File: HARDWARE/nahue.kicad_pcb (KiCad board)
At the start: 2 copper layers, 42 parts, among them J1 Conn_01x15, J2 Screw_Terminal_01x03, J3 Screw_Terminal_01x03, J4 Screw_Terminal_01x03, J5 bateria, J6 Screw_Terminal_01x03, J7 Conn_01x15, K1 JQC-3FF-005-1Z, K2 JQC-3FF-005-1Z, K3 JQC-3FF-005-1Z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

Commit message: actualizacion de kicad
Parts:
- added U6: LM7805_TO220, Package_TO_SOT_THT:TO-220-3_Vertical, F.Cu at (98.7, 20.2)
- J2, J3, J4, J5, J6, K1, K2, K3, K4: moved to F.Cu
- U5: value KA78M05_TO252 -> ESP32-S2-WROVER; footprint Package_TO_SOT_SMD:TO-252-2 -> RF_Module:ESP32-S2-WROVER; moved to F.Cu
- moved U5 152.8 mm to (18.4, 29.9)
- moved J5 95.2 mm to (86.5, 25.2)
- moved K3 74.6 mm to (110.0, 109.0)
- moved J4 72.6 mm to (86.9, 108.0), turned to 90 degrees
- moved D1 67.2 mm to (127.8, 100.8), turned to 0 degrees
- moved D2 66.4 mm to (117.0, 103.2), turned to 90 degrees
- moved R3 65.8 mm to (122.4, 100.8)
- moved Q3 63.1 mm to (122.4, 105.5)
- moved R2 62.9 mm to (128.3, 104.6)
- moved U3 62.1 mm to (139.7, 102.0), turned to 180 degrees
- moved R10 57.4 mm to (148.4, 43.9), turned to 180 degrees
- moved R1 57.2 mm to (148.4, 100.8), turned to 180 degrees
- moved R11 53.8 mm to (127.9, 47.8)
- moved Q1 53.8 mm to (122.4, 48.7)
- moved U1 53.3 mm to (138.9, 45.2), turned to 180 degrees
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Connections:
- C1 pad 1: VIN -> Net-(J5-Pin_2)
- C1 pad 2: GND -> Net-(U6-VI)
- R10 pad 1: D21 -> D22
- R4 pad 2: D5 -> D19
- R7 pad 2: D19 -> D21
- U5 pad 1: Net-(J5-Pin_2) -> Net-(U5-GND-Pad1)
- U5 pad 2: GND -> unconnected-(U5-3V3-Pad2)
- U5 pad 3: VIN -> unconnected-(U5-IO00-Pad3)
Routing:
- net VIN: track 229.6 -> 445.2 mm
- net D18: track 0.00 -> 58.6 mm
- net Net-(J5-Pin_2): track 18.1 -> 68.9 mm
- net D19: track 0.00 -> 43.3 mm
- net Net-(U6-VI): track 0.00 -> 32.8 mm
- net D21: track 0.00 -> 32.2 mm
- net D22: track 0.00 -> 23.9 mm
- net Net-(D4-A): track 34.0 -> 18.9 mm
- net Net-(D6-A): track 34.0 -> 18.9 mm
- net Net-(D2-A): track 33.4 -> 19.4 mm
- net Net-(D8-A): track 32.9 -> 19.0 mm
- net GND: track 9.51 -> 18.7 mm
- net COM2: track 35.2 -> 30.1 mm
- net COM3: track 34.2 -> 30.1 mm
- net Net-(R8-Pad1): track 10.1 -> 6.39 mm
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
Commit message: modificacion del kicad
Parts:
- removed U5: ESP32-S2-WROVER, RF_Module:ESP32-S2-WROVER

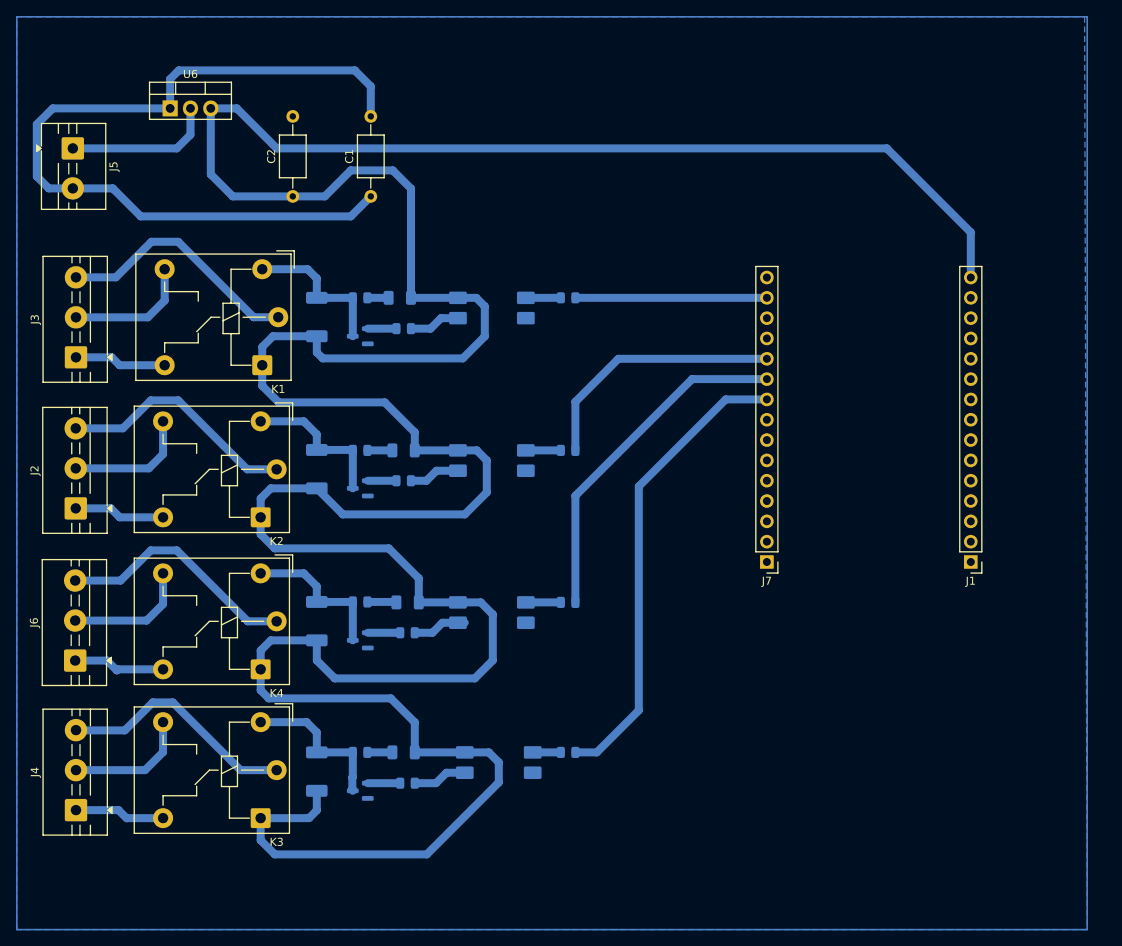
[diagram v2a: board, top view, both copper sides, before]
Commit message: se agrego huella del ESP32(falta terminar)
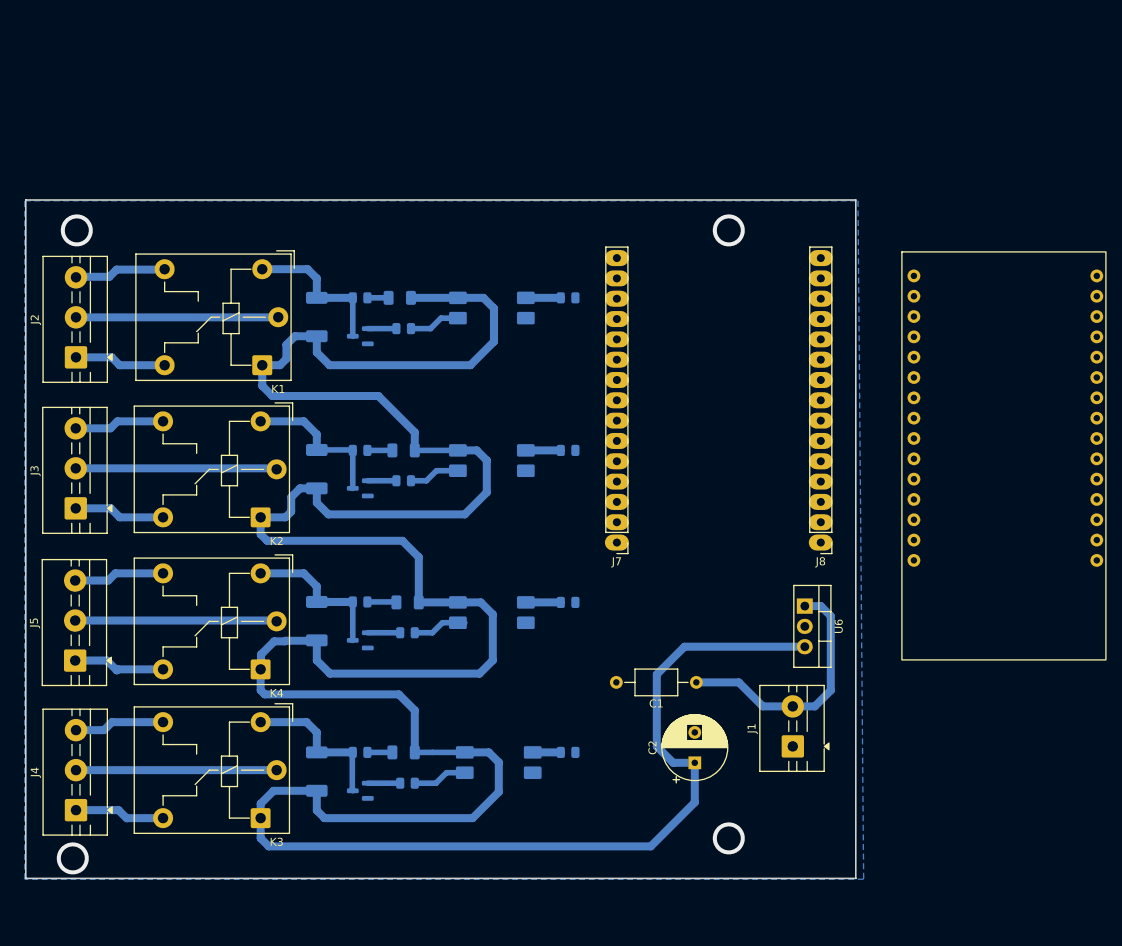
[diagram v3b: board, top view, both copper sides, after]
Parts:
- removed the J5 at (86.5, 25.2)
- added J1: ~, TerminalBlock:TerminalBlock_MaiXu_MX126-5.0-02P_1x02_P5.00mm, F.Cu at (176.5, 100.0)
- added U5: ~, esp32-30pines:esp32, F.Cu at (191.6, 41.2)
- C1: value C_Small -> ~
- C2: value C_Small -> ~; footprint Capacitor_THT:C_Axial_L5.1mm_D3.1mm_P10.00mm_Horizontal -> Capacitor_THT:CP_Radial_D8.0mm_P3.80mm
- J3: renamed from J2; value Screw_Terminal_01x03 -> ~
- moved U6 100.8 mm to (178.0, 82.5), turned to -90 degrees
- moved C2 86.8 mm to (164.2, 102.1)
- moved C1 73.1 mm to (164.4, 92.0), turned to 180 degrees
- moved J7 18.9 mm to (154.5, 74.5)
- moved J8 18.9 mm to (180.0, 74.5)
- renumbered J3 to J2, J6 to J5, J1 to J8
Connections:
- C1 pad 1: Net-(J5-Pin_2) -> Net-(J1-Pin_2)
- C1 pad 2: Net-(U6-VI) -> GND
- J2 pad 2: NC1 -> COM1
- J2 pad 3: COM1 -> NC1
- J3 pad 2: NC2 -> COM2
- J3 pad 3: COM2 -> NC2
- J4 pad 2: NC3 -> COM3
- J4 pad 3: COM3 -> NC3
- J5 pad 2: NC4 -> COM4
- J5 pad 3: COM4 -> NC4
- R10 pad 1: D22 -> TX0
- R7 pad 2: D21 -> RX0
- U6 pad 1: Net-(U6-VI) -> Net-(J1-Pin_2)
- U6 pad 3: Net-(U6-VO) -> VIN
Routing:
- net Net-(J5-Pin_2): track 68.9 -> 0.00 mm
- net VIN: track 445.2 -> 383.6 mm
- net D18: track 58.6 -> 0.00 mm
- net D19: track 43.3 -> 0.00 mm
- net Net-(U6-VI): track 32.8 -> 0.00 mm
- net D21: track 32.2 -> 0.00 mm
- net Net-(J1-Pin_2): track 0.00 -> 31.9 mm
- net D22: track 23.9 -> 0.00 mm
- net GND: track 18.7 -> 0.00 mm, vias 0 -> 4
- net COM1: track 31.0 -> 25.3 mm
- net COM4: track 30.4 -> 25.2 mm
- net COM3: track 30.1 -> 25.1 mm
- net COM2: track 30.1 -> 25.2 mm
- net NC1: track 15.9 -> 11.4 mm
- net NC2: track 15.8 -> 11.3 mm
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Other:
- board outline added: 103.8 x 84.8 mm

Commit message: últimos arreglos 1
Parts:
- removed J7, J8: Conn_01x15, Connector_PinHeader_2.54mm:PinHeader_1x15_P2.54mm_Vertical
- moved U5 37.6 mm to (174.4, 74.6), turned to 180 degrees
- moved C2 9.78 mm to (154.6, 103.8)
- moved J1 9.78 mm to (166.9, 101.8)
- moved U6 9.78 mm to (168.4, 84.2)
- moved R7 8.07 mm to (141.8, 58.5), turned to 90 degrees
- moved R4 6.97 mm to (143.1, 77.5), turned to 90 degrees
- moved R10 6.93 mm to (143.1, 39.4), turned to -90 degrees
- moved C1 6.92 mm to (157.8, 94.0), turned to 90 degrees
- moved R1 6.45 mm to (144.0, 96.1), turned to -90 degrees
- moved D6 3.82 mm to (118.1, 69.0)
- moved U2 1.38 mm to (137.5, 64.3)
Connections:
- R10 pad 1: TX0 -> RX2
- R7 pad 2: RX0 -> DX2
- U5 pad 1: unconnected-(U5-3V3-Pad1) -> EN
- U5 pad 10: unconnected-(U5-D19-Pad10) -> D27
- U5 pad 11: unconnected-(U5-D14-Pad11) -> D14
- U5 pad 12: unconnected-(U5-D12-Pad12) -> D12
- U5 pad 13: TX0 -> D13
- U5 pad 14: unconnected-(U5-D22-Pad14) -> GND
- U5 pad 15: unconnected-(U5-D23-Pad15) -> VIN
- U5 pad 2: unconnected-(U5-GND-Pad2) -> VP
- U5 pad 3: unconnected-(U5-D15-Pad3) -> VN
- U5 pad 4: unconnected-(U5-D2-Pad4) -> D34
- U5 pad 5: unconnected-(U5-D4-Pad5) -> D35
- U5 pad 6: unconnected-(U5-D32-Pad6) -> D32
- U5 pad 7: unconnected-(U5-D33-Pad7) -> D33
- U5 pad 8: unconnected-(U5-D5-Pad8) -> D25
- U5 pad 9: unconnected-(U5-D18-Pad9) -> D26
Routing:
- net D18: track 0.00 -> 45.0 mm
- net VIN: track 383.6 -> 414.1 mm
- net D19: track 0.00 -> 27.5 mm
- net RX2: track 0.00 -> 17.9 mm
- net DX2: track 0.00 -> 9.60 mm
- net Net-(D6-A): track 18.9 -> 24.8 mm
- net Net-(J1-Pin_2): track 31.9 -> 30.0 mm
- net Net-(R8-Pad1): track 6.39 -> 5.00 mm
- net Net-(R10-Pad2): track 4.37 -> 3.58 mm
- net Net-(R4-Pad1): track 4.37 -> 3.63 mm
- net Net-(R7-Pad1): track 4.37 -> 3.63 mm
- net GND: vias 4 -> 0
- net (no net): vias 0 -> 3
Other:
- board size 103.8 x 84.8 mm -> 97.2 x 84.8 mm

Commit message: retoques del kicad
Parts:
- moved D6 3.82 mm to (117.0, 65.3)
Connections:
- R10 pad 1: RX2 -> RX0
- R7 pad 2: DX2 -> TX0
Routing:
- net RX0: track 0.00 -> 32.4 mm
- net TX0: track 0.00 -> 23.9 mm
- net RX2: track 17.9 -> 0.00 mm
- net DX2: track 9.60 -> 0.00 mm
- net Net-(D6-A): track 24.8 -> 18.9 mm
- net VIN: track 414.1 -> 416.8 mm
- net D19: track 27.5 -> 26.3 mm
- net Net-(J1-Pin_2): track 30.0 -> 28.8 mm

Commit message: finalizando
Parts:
- added J6: Conn_01x08, Connector_PinSocket_2.54mm:PinSocket_1x08_P2.54mm_Vertical, F.Cu at (152.5, 81.8)
- K1, K2, K3, K4: value JQC-3FF-005-1Z -> RELAY
- moved U6 28.7 mm to (169.7, 112.8), turned to 180 degrees
- moved J1 17.3 mm to (153.7, 113.0), turned to 0 degrees
- moved C1 16.7 mm to (169.7, 105.8), turned to 180 degrees
- moved C2 11.8 mm to (147.0, 112.8), turned to 180 degrees
- moved R4 3.73 mm to (139.4, 77.5)
- moved R7 3.68 mm to (139.1, 55.9), turned to 0 degrees
- moved U2 3.01 mm to (134.8, 63.1), turned to -90 degrees
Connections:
- R1 pad 1: D18 -> D19
- R10 pad 1: RX0 -> RX2
- R4 pad 2: D19 -> D18
- R7 pad 2: TX0 -> DX2
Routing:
- net D2: track 0.00 -> 46.4 mm
- net D25: track 0.00 -> 32.4 mm
- net D32: track 0.00 -> 25.2 mm
- net D18: track 44.5 -> 24.0 mm
- net RX2: track 0.00 -> 17.7 mm
- net D22: track 0.00 -> 14.5 mm
- net VIN: track 416.8 -> 430.8 mm
- net VP: track 0.00 -> 13.1 mm
- net D19: track 26.3 -> 38.7 mm
- net DX2: track 0.00 -> 9.55 mm
- net RX0: track 32.4 -> 24.2 mm
- net Net-(J1-Pin_2): track 28.8 -> 22.5 mm
- net Net-(R8-Pad1): track 5.00 -> 11.1 mm
- net TX0: track 23.9 -> 19.6 mm
- net Net-(R7-Pad1): track 3.63 -> 7.46 mm
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- added copper zone on B.Cu, net (none)
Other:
- board size 97.2 x 84.8 mm -> 97.2 x 86.4 mm

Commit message: finalizado 2
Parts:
- added SW1: SW, Connector_PinHeader_2.54mm:PinHeader_1x02_P2.54mm_Vertical, F.Cu at (172.0, 97.8)
- moved J1 18.4 mm to (172.0, 110.8), turned to 90 degrees
- moved C2 9.82 mm to (152.6, 104.8)
- moved C1 8.10 mm to (162.8, 101.5), turned to 90 degrees
- moved U6 7.21 mm to (162.8, 110.8)
- moved R7 4.89 mm to (143.1, 58.7), turned to 90 degrees
- moved U2 4.31 mm to (138.9, 64.3), turned to 180 degrees
- moved R4 3.85 mm to (143.2, 77.7)
- moved R10 1.53 mm to (142.1, 40.6), turned to 0 degrees
- moved U4 0.12 mm to (139.0, 83.3)
- moved J5 0.10 mm to (86.9, 89.3)
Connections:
- C1 pad 1: Net-(J1-Pin_2) -> Net-(SW1A-B)
- R1 pad 1: D19 -> D23
- R4 pad 2: D18 -> D19
- U6 pad 1: Net-(J1-Pin_2) -> Net-(SW1A-B)
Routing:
- net D18: track 24.0 -> 0.00 mm
- net VIN: track 430.8 -> 407.2 mm
- net D23: track 0.00 -> 22.6 mm
- net D19: track 38.7 -> 18.2 mm
- net Net-(SW1A-B): track 0.00 -> 19.0 mm
- net Net-(J1-Pin_2): track 22.5 -> 8.01 mm
- net Net-(R8-Pad1): track 11.1 -> 6.37 mm
- net Net-(R7-Pad1): track 7.46 -> 3.42 mm
- net RX2: track 17.7 -> 21.1 mm
- net Net-(R4-Pad1): track 6.57 -> 3.42 mm
- net DX2: track 9.55 -> 8.30 mm
- net (no net): vias 2 -> 4

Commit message: duplicacion de placa
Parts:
- added C1: ~, Capacitor_THT:C_Axial_L5.1mm_D3.1mm_P10.00mm_Horizontal, F.Cu at (242.1, 130.2)
- added C2: ~, Capacitor_THT:CP_Radial_D8.0mm_P3.80mm, F.Cu at (231.9, 133.4)
- added D1: led smd 1206, LED_SMD:LED_1206_3216Metric, B.Cu at (207.2, 129.4)
- added D2: SM4007, Diode_SMD:D_MELF, B.Cu at (196.3, 131.8)
- added D3: led smd 1206, LED_SMD:LED_1206_3216Metric, B.Cu at (207.7, 110.7)
- added D4: SM4007, Diode_SMD:D_MELF, B.Cu at (196.3, 113.0)
- added D5: led smd 1206, LED_SMD:LED_1206_3216Metric, B.Cu at (207.2, 91.7)
- added D6: SM4007, Diode_SMD:D_MELF, B.Cu at (196.3, 94.0)
- added D7: led smd 1206, LED_SMD:LED_1206_3216Metric, B.Cu at (206.7, 72.6)
- added D8: SM4007, Diode_SMD:D_MELF, B.Cu at (196.3, 75.0)
- added J1: ~, TerminalBlock:TerminalBlock_MaiXu_MX126-5.0-02P_1x02_P5.00mm, F.Cu at (251.3, 139.4)
- added J2: Screw_Terminal_01x03, TerminalBlock:TerminalBlock_MaiXu_MX126-5.0-03P_1x03_P5.00mm, F.Cu at (166.2, 80.0)
- added J3: ~, TerminalBlock:TerminalBlock_MaiXu_MX126-5.0-03P_1x03_P5.00mm, F.Cu at (166.2, 98.9)
- added J4: Screw_Terminal_01x03, TerminalBlock:TerminalBlock_MaiXu_MX126-5.0-03P_1x03_P5.00mm, F.Cu at (166.2, 136.6)
- added J5: Screw_Terminal_01x03, TerminalBlock:TerminalBlock_MaiXu_MX126-5.0-03P_1x03_P5.00mm, F.Cu at (166.2, 117.9)
- added J6: Conn_01x08, Connector_PinSocket_2.54mm:PinSocket_1x08_P2.54mm_Vertical, F.Cu at (231.8, 110.5)
- added K1: RELAY, Relay_THT:Relay_SPDT_Hongfa_JQC-3FF_0XX-1Z, F.Cu at (189.5, 81.0)
- added K2: RELAY, Relay_THT:Relay_SPDT_Hongfa_JQC-3FF_0XX-1Z, F.Cu at (189.3, 100.0)
- added K3: RELAY, Relay_THT:Relay_SPDT_Hongfa_JQC-3FF_0XX-1Z, F.Cu at (189.3, 137.6)
- added K4: RELAY, Relay_THT:Relay_SPDT_Hongfa_JQC-3FF_0XX-1Z, F.Cu at (189.3, 119.0)
- added Q1: MMBT3904, Package_TO_SOT_SMD:SOT-23, B.Cu at (201.8, 77.4)
- added Q2: MMBT3904, Package_TO_SOT_SMD:SOT-23, B.Cu at (201.8, 96.4)
- added Q3: MMBT3904, Package_TO_SOT_SMD:SOT-23, B.Cu at (201.8, 134.2)
- added Q4: MMBT3904, Package_TO_SOT_SMD:SOT-23, B.Cu at (201.8, 115.4)
- added R1: 220, Resistor_SMD:R_0805_2012Metric, B.Cu at (223.3, 124.7)
- added R10: 220, Resistor_SMD:R_0805_2012Metric, B.Cu at (221.5, 69.2)
- added R11: 1k, Resistor_SMD:R_0805_2012Metric, B.Cu at (207.2, 76.4)
- added R12: 220, Resistor_SMD:R_0805_2012Metric, B.Cu at (201.7, 72.6)
- added R2: 1k, Resistor_SMD:R_0805_2012Metric, B.Cu at (207.7, 133.2)
- added R3: 220, Resistor_SMD:R_0805_2012Metric, B.Cu at (201.7, 129.4)
- added R4: 220, Resistor_SMD:R_0805_2012Metric, B.Cu at (222.6, 106.3)
- added R5: 1k, Resistor_SMD:R_0805_2012Metric, B.Cu at (207.7, 114.4)
- added R6: 220, Resistor_SMD:R_0805_2012Metric, B.Cu at (201.7, 110.6)
- added R7: 220, Resistor_SMD:R_0805_2012Metric, B.Cu at (222.5, 87.3)
- added R8: 1k, Resistor_SMD:R_0805_2012Metric, B.Cu at (207.2, 95.4)
- added R9: 220, Resistor_SMD:R_0805_2012Metric, B.Cu at (201.7, 91.7)
- added SW1: SW, Connector_PinHeader_2.54mm:PinHeader_1x02_P2.54mm_Vertical, F.Cu at (251.3, 126.4)
- added U1: PC817, PC817SMD:SOIC254P1000X400-4N, B.Cu at (218.2, 73.8)
- added U2: PC817, PC817SMD:SOIC254P1000X400-4N, B.Cu at (218.2, 92.9)
- added U3: PC817, PC817SMD:SOIC254P1000X400-4N, B.Cu at (219.1, 130.7)
- added U4: PC817, PC817SMD:SOIC254P1000X400-4N, B.Cu at (218.3, 111.9)
- added U5: ~, esp32-30pines:esp32, F.Cu at (253.7, 103.3)
- added U6: LM7805_TO220, Package_TO_SOT_THT:TO-220-3_Vertical, F.Cu at (242.1, 139.4)
- moved C1 48.4 mm to (123.0, 129.2)
- moved C2 48.4 mm to (112.9, 132.4)
- moved J4 48.4 mm to (47.2, 135.6)
- moved K3 48.4 mm to (70.3, 136.6)
- moved R2 48.4 mm to (88.6, 132.3)
- moved R4 48.4 mm to (103.5, 105.3)
- moved U5 48.4 mm to (134.7, 102.3)
- moved U6 48.4 mm to (123.0, 138.4)
- moved D7 48.4 mm to (87.7, 71.6)
- moved J2 48.4 mm to (47.2, 79.0)
- moved K1 48.4 mm to (70.5, 80.0)
- moved Q1 48.4 mm to (82.7, 76.4)
- moved D1 48.4 mm to (88.2, 128.4)
- moved D2 48.4 mm to (77.3, 130.8)
- moved D4 48.4 mm to (77.3, 112.0)
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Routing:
- net VIN: track 407.2 -> 814.4 mm
- net D2: track 46.4 -> 92.8 mm
- net D25: track 32.4 -> 64.7 mm
- net COM1: track 25.3 -> 50.6 mm
- net D32: track 25.2 -> 50.5 mm
- net COM4: track 25.2 -> 50.4 mm
- net COM2: track 25.2 -> 50.3 mm
- net COM3: track 25.1 -> 50.2 mm
- net RX0: track 24.2 -> 48.4 mm
- net D23: track 22.6 -> 45.1 mm
- net RX2: track 21.1 -> 42.1 mm
- net TX0: track 19.6 -> 39.2 mm
- net Net-(D2-A): track 19.4 -> 38.8 mm
- net Net-(D8-A): track 19.0 -> 38.0 mm
- net Net-(SW1A-B): track 19.0 -> 38.0 mm
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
